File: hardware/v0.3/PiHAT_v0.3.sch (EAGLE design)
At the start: 37 parts, among them IC1 BMP280, J1 FTDI, J3 ISP, U1 ATMEGA328P, U2 TSL2561, U3 OPA344, U6 ADMP401, U7 SHT31/35, U8 CCS811, Y1 16MHZ

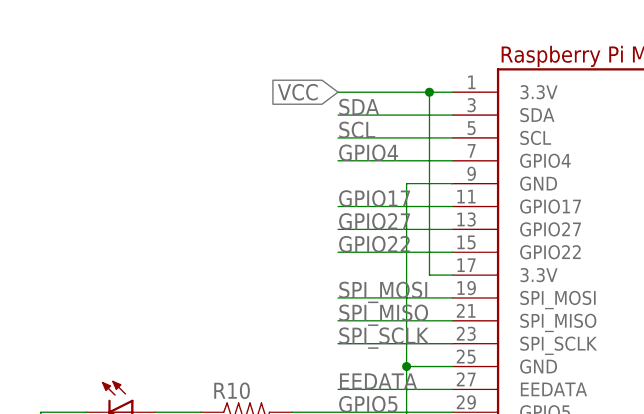
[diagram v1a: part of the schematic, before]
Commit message: Added jumpers on the I2C line
Jumpers between Pi's SDA and SCL lines and ATmega's SDA and SCL lines
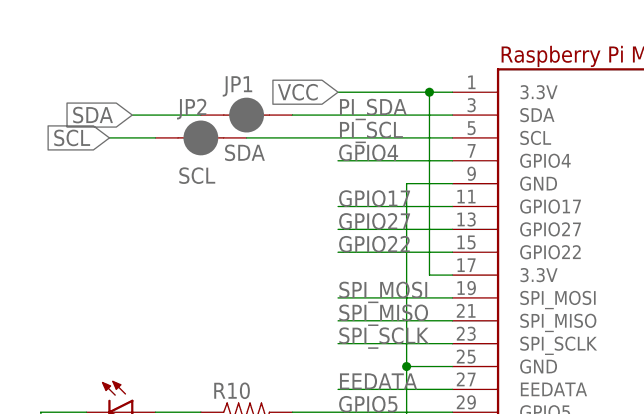
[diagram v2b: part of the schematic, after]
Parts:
- added JP1: SDA, SparkFun-Passives:JUMPER-PAD-2-NC_BY_PASTEFULL-BOX-SILK
- added JP2: SCL, SparkFun-Passives:JUMPER-PAD-2-NC_BY_PASTEFULL-BOX-SILK
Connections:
- new net PI_SCL: JP2.2, RPI1.SCL
- new net PI_SDA: JP1.2, RPI1.SDA
- net SCL: now also JP2.1; no longer RPI1.SCL
- net SDA: now also JP1.1; no longer RPI1.SDA
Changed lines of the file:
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@@
 <part name="C1" library="SparkFun-Passives" deviceset="CAP" device="0805" value="0.1uF"/>
 <part name="C6" library="SparkFun-Passives" deviceset="CAP" device="0805" value="0.1uF"/>
+<part name="JP1" library="SparkFun-Passives" deviceset="JUMPER-PAD-2-NC_BY_PASTE" device="FULL-BOX-SILK" value="SDA"/>
+<part name="JP2" library="SparkFun-Passives" deviceset="JUMPER-PAD-2-NC_BY_PASTE" device="FULL-BOX-SILK" value="SCL"/>
 </parts>
 <sheets>
@@
 <instance part="C1" gate="G$1" x="353.06" y="99.06"/>
 <instance part="C6" gate="G$1" x="289.56" y="104.14" rot="R180"/>
+<instance part="JP1" gate="G$1" x="182.88" y="121.92"/>
+<instance part="JP2" gate="G$1" x="177.8" y="119.38"/>
 </instances>
 <busses>
@@
 </segment>
 <segment>
-<pinref part="RPI1" gate="G$1" pin="SDA"/>
-<wire x1="205.74" y1="121.92" x2="193.04" y2="121.92" width="0.1524" layer="91"/>
-<label x="193.04" y="121.92" size="1.778" layer="95"/>
+<pinref part="JP1" gate="G$1" pin="1"/>
+<wire x1="177.8" y1="121.92" x2="170.18" y2="121.92" width="0.1524" layer="91"/>
+<label x="170.18" y="121.92" size="1.778" layer="95" rot="R180" xref="yes"/>
 </segment>
 </net>
@@
 </segment>
 <segment>
-<pinref part="RPI1" gate="G$1" pin="SCL"/>
-<wire x1="205.74" y1="119.38" x2="193.04" y2="119.38" width="0.1524" layer="91"/>
-<label x="193.04" y="119.38" size="1.778" layer="95"/>
+<pinref part="JP2" gate="G$1" pin="1"/>
+<wire x1="172.72" y1="119.38" x2="167.64" y2="119.38" width="0.1524" layer="91"/>
+<label x="167.64" y="119.38" size="1.778" layer="95" rot="R180" xref="yes"/>
 </segment>
 </net>
@@
 </segment>
 </net>
+<net name="PI_SDA" class="0">
+<segment>
+<pinref part="RPI1" gate="G$1" pin="SDA"/>
+<wire x1="205.74" y1="121.92" x2="187.96" y2="121.92" width="0.1524" layer="91"/>
+<label x="193.04" y="121.92" size="1.778" layer="95"/>
+<pinref part="JP1" gate="G$1" pin="2"/>
+</segment>
+</net>
+<net name="PI_SCL" class="0">
+<segment>
+<pinref part="RPI1" gate="G$1" pin="SCL"/>
+<wire x1="205.74" y1="119.38" x2="182.88" y2="119.38" width="0.1524" layer="91"/>
+<label x="193.04" y="119.38" size="1.778" layer="95"/>
+<pinref part="JP2" gate="G$1" pin="2"/>
+</segment>
+</net>

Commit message: BOM adjustments
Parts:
- removed C6: 0.1uF, SparkFun-Passives:CAP0805
- added C7: 0.1uF, SparkFun-Passives:CAP0805
- C11: DIGIKEY# (none) -> 311-1088-1-ND; MOUSER# (none) -> 603-CC603KRX7R7BB104; MPN (none) -> CC0603KRX7R7BB104
- C3: MOUSER# 603-RC0805FR-07100RL -> 603-CC603KRX7R7BB104
- renumbered C1 to C11
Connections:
- net GND: now also C7.2; no longer C6.1
- net VCC: now also C7.1; no longer C6.2
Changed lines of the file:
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@@
 <?xml version="1.0" encoding="utf-8"?>
 <!DOCTYPE eagle SYSTEM "eagle.dtd">
-<eagle version="7.7.0">
+<eagle version="7.6.0">
 <drawing>
 <settings>
@@
 <part name="C3" library="SparkFun-Passives" deviceset="CAP" device="0805" value="0.1uF">
 <attribute name="DIGIKEY#" value="311-1088-1-ND"/>
-<attribute name="MOUSER#" value="603-RC0805FR-07100RL"/>
+<attribute name="MOUSER#" value="603-CC603KRX7R7BB104"/>
 <attribute name="MPN" value="CC0603KRX7R7BB104"/>
 </part>
@@
 <part name="SUPPLY10" library="SparkFun-Aesthetics" deviceset="VCC" device=""/>
 <part name="SUPPLY13" library="SparkFun-Aesthetics" deviceset="VCC" device=""/>
-<part name="C1" library="SparkFun-Passives" deviceset="CAP" device="0805" value="0.1uF"/>
-<part name="C6" library="SparkFun-Passives" deviceset="CAP" device="0805" value="0.1uF"/>
 <part name="JP1" library="SparkFun-Passives" deviceset="JUMPER-PAD-2-NC_BY_PASTE" device="FULL-BOX-SILK" value="SDA"/>
 <part name="JP2" library="SparkFun-Passives" deviceset="JUMPER-PAD-2-NC_BY_PASTE" device="FULL-BOX-SILK" value="SCL"/>
+<part name="C7" library="SparkFun-Passives" deviceset="CAP" device="0805" value="0.1uF">
+<attribute name="DIGIKEY#" value="311-1088-1-ND"/>
+<attribute name="MOUSER#" value="603-CC603KRX7R7BB104"/>
+<attribute name="MPN" value="CC0603KRX7R7BB104"/>
+</part>
+<part name="C11" library="SparkFun-Passives" deviceset="CAP" device="0805" value="0.1uF">
+<attribute name="DIGIKEY#" value="311-1088-1-ND"/>
+<attribute name="MOUSER#" value="603-CC603KRX7R7BB104"/>
+<attribute name="MPN" value="CC0603KRX7R7BB104"/>
+</part>
 </parts>
 <sheets>
@@
 <instance part="SUPPLY10" gate="G$1" x="353.06" y="114.3"/>
 <instance part="SUPPLY13" gate="G$1" x="289.56" y="114.3"/>
-<instance part="C1" gate="G$1" x="353.06" y="99.06"/>
-<instance part="C6" gate="G$1" x="289.56" y="104.14" rot="R180"/>
 <instance part="JP1" gate="G$1" x="182.88" y="121.92"/>
 <instance part="JP2" gate="G$1" x="177.8" y="119.38"/>
+<instance part="C7" gate="G$1" x="289.56" y="101.6">
+<attribute name="DIGIKEY#" x="289.56" y="101.6" size="1.778" layer="96" display="off"/>
+<attribute name="MPN" x="289.56" y="101.6" size="1.778" layer="96" display="off"/>
+<attribute name="MOUSER#" x="289.56" y="101.6" size="1.778" layer="96" display="off"/>
+</instance>
+<instance part="C11" gate="G$1" x="353.06" y="99.06">
+<attribute name="DIGIKEY#" x="353.06" y="99.06" size="1.778" layer="96" display="off"/>
+<attribute name="MPN" x="353.06" y="99.06" size="1.778" layer="96" display="off"/>
+<attribute name="MOUSER#" x="353.06" y="99.06" size="1.778" layer="96" display="off"/>
+</instance>
 </instances>
 <busses>
@@
 <segment>
 <pinref part="IC1" gate="G$1" pin="GND"/>
-<pinref part="C6" gate="G$1" pin="1"/>
 <wire x1="297.18" y1="99.06" x2="289.56" y2="99.06" width="0.1524" layer="91"/>
 <wire x1="289.56" y1="99.06" x2="289.56" y2="91.44" width="0.1524" layer="91"/>
-<junction x="289.56" y="99.06"/>
 <wire x1="353.06" y1="91.44" x2="312.42" y2="91.44" width="0.1524" layer="91"/>
 <wire x1="312.42" y1="91.44" x2="289.56" y2="91.44" width="0.1524" layer="91"/>
@@
 <junction x="312.42" y="91.44"/>
 <label x="312.42" y="86.36" size="1.778" layer="95" rot="R270" xref="yes"/>
-<pinref part="C1" gate="G$1" pin="2"/>
 <wire x1="353.06" y1="91.44" x2="353.06" y2="96.52" width="0.1524" layer="91"/>
+<pinref part="C7" gate="G$1" pin="2"/>
+<junction x="289.56" y="99.06"/>
+<pinref part="C11" gate="G$1" pin="2"/>
 </segment>
 </net>
@@
 <wire x1="297.18" y1="109.22" x2="289.56" y2="109.22" width="0.1524" layer="91"/>
 <wire x1="289.56" y1="109.22" x2="289.56" y2="114.3" width="0.1524" layer="91"/>
-<pinref part="C6" gate="G$1" pin="2"/>
 <wire x1="289.56" y1="106.68" x2="289.56" y2="109.22" width="0.1524" layer="91"/>
 <junction x="289.56" y="109.22"/>
+<pinref part="C7" gate="G$1" pin="1"/>
 </segment>
 <segment>
@@
 <pinref part="SUPPLY10" gate="G$1" pin="VCC"/>
 <wire x1="353.06" y1="109.22" x2="353.06" y2="114.3" width="0.1524" layer="91"/>
-<pinref part="C1" gate="G$1" pin="1"/>
 <wire x1="353.06" y1="104.14" x2="353.06" y2="109.22" width="0.1524" layer="91"/>
 <junction x="353.06" y="109.22"/>
-</segment>
-</net>
+<pinref part="C11" gate="G$1" pin="1"/>
+</segment>
+</net>

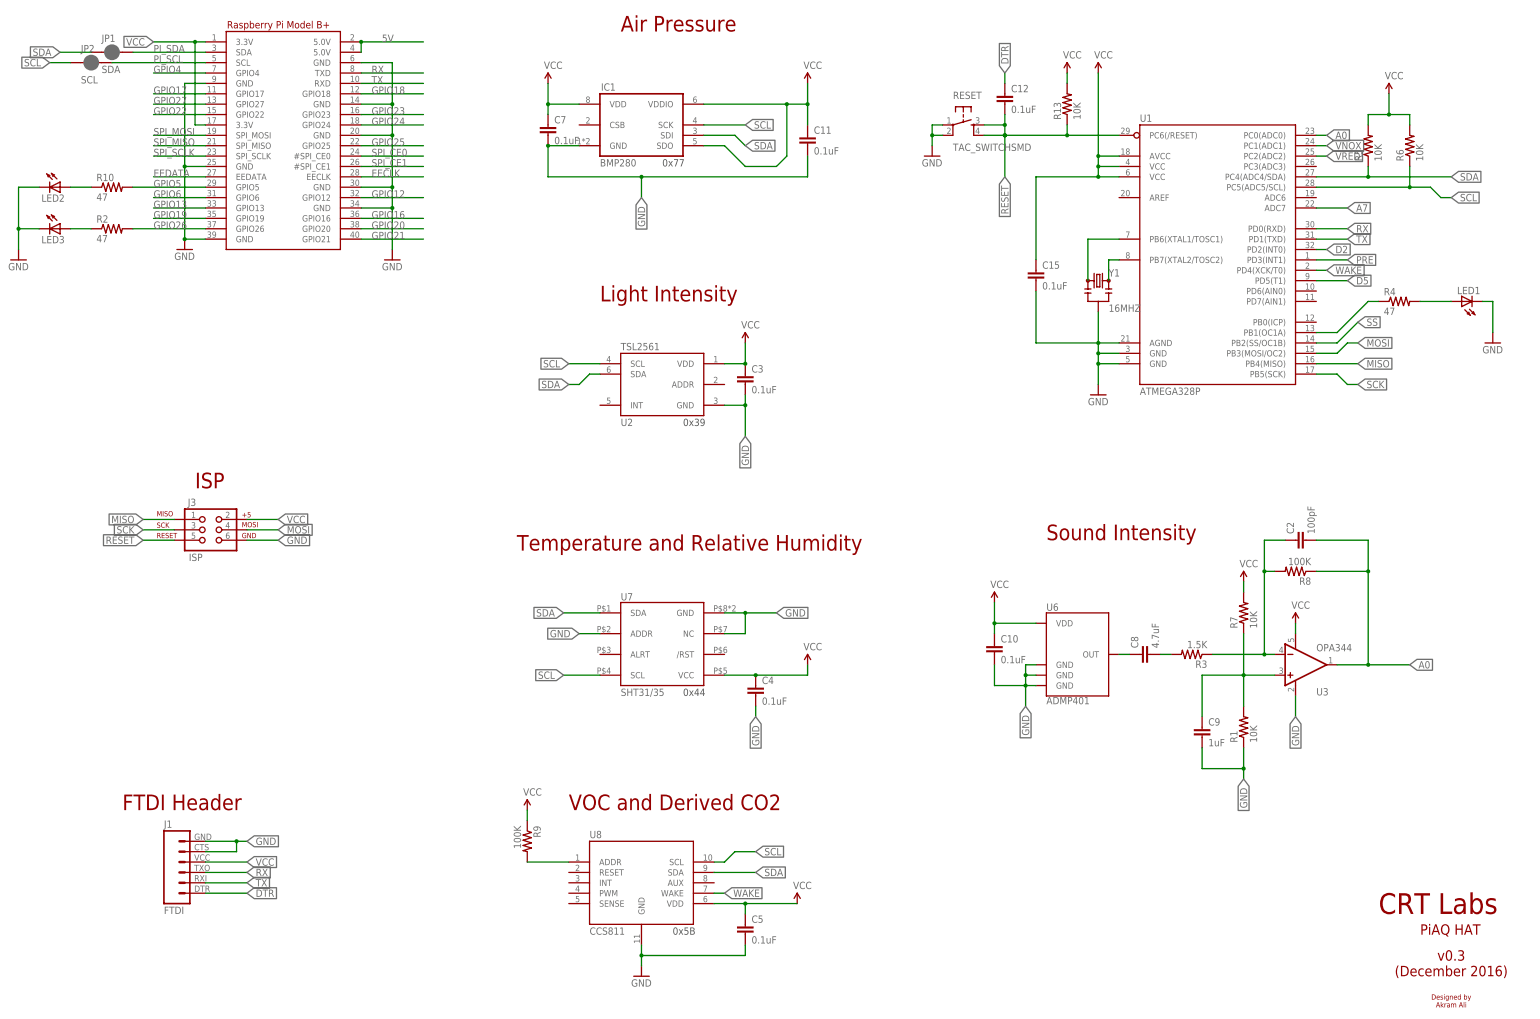
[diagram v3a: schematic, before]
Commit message: Updated all attributes for BOM
Fixed digikey and mouser numbers
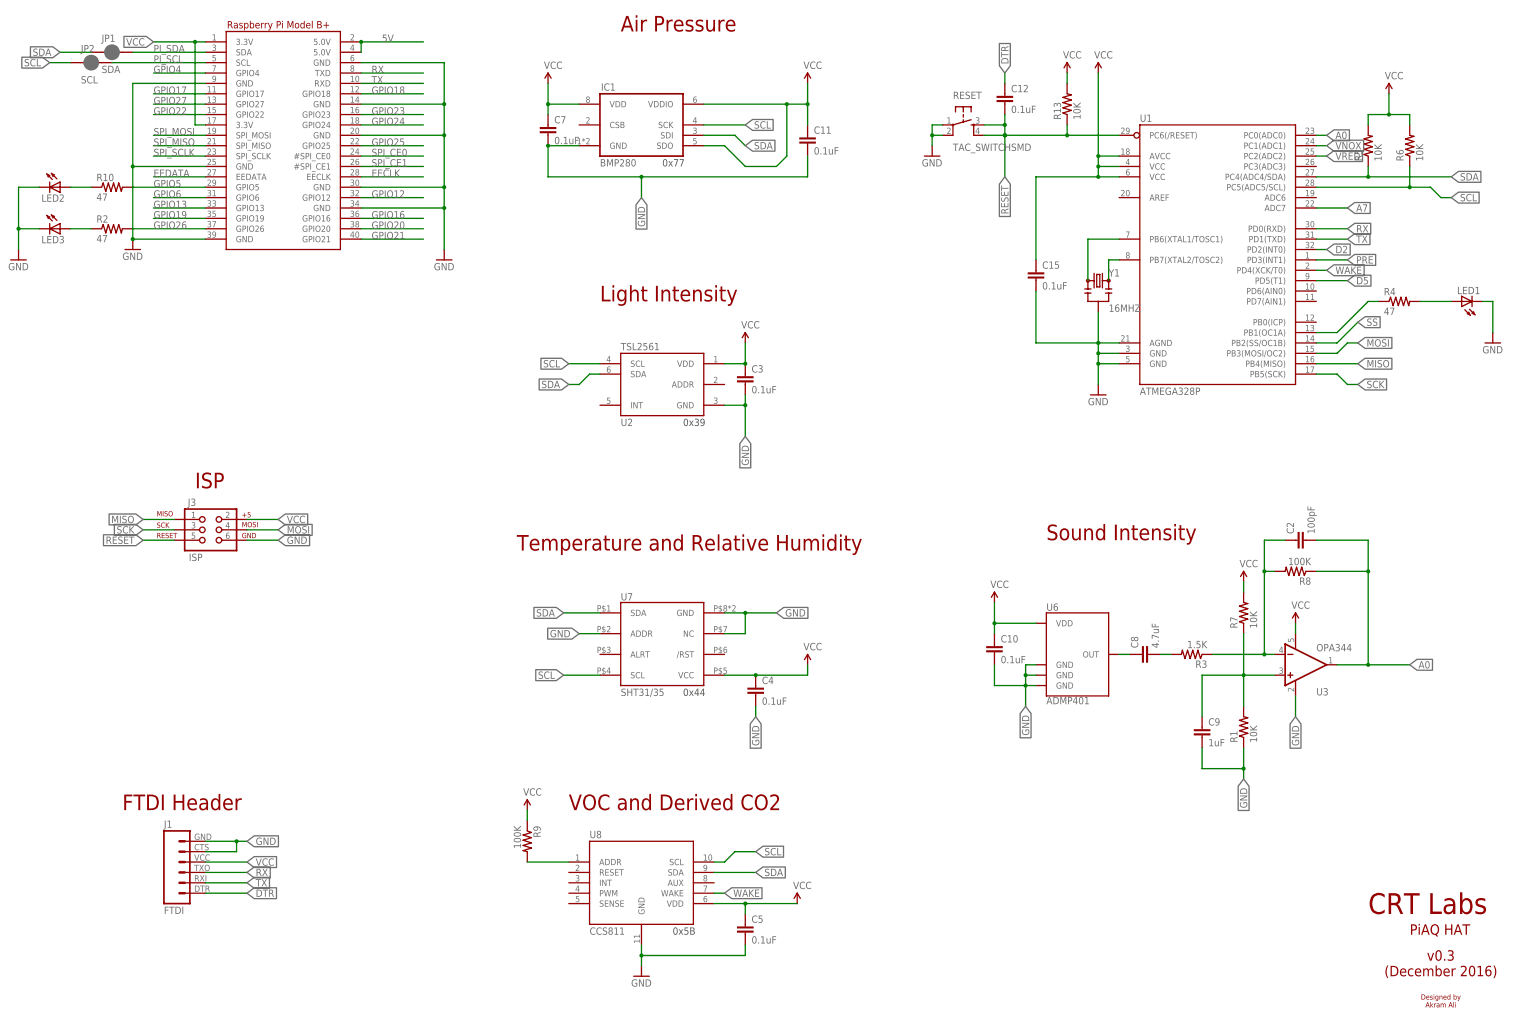
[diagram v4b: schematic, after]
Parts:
- IC1: DIGIKEY# (none) -> 828-1064-1-ND; MANF (none) -> BMP280; MOUSER# (none) -> 262-BMP280
- J1: DIGIKEY# 768-1129-1-ND -> (none); MOUSER# 895-FT231XS-R -> (none); MPN FT231XS-R -> (none); NO_BOM (none) -> TRUE
- R8, R9: DIGIKEY# 541-82.0CCT-ND -> 311-100KCRCT-ND
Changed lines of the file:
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@@
 </part>
 <part name="R8" library="SparkFun-Passives" deviceset="RESISTOR" device="0805-RES" value="100K">
-<attribute name="DIGIKEY#" value="541-82.0CCT-ND"/>
+<attribute name="DIGIKEY#" value="311-100KCRCT-ND"/>
 <attribute name="MOUSER#" value="603-RC0805FR-07100KL"/>
 <attribute name="MPN" value="RC0805FR-07100KL"/>
@@
 <part name="SUPPLY8" library="SparkFun-Aesthetics" deviceset="VCC" device=""/>
 <part name="R9" library="SparkFun-Passives" deviceset="RESISTOR" device="0805-RES" value="100K">
-<attribute name="DIGIKEY#" value="541-82.0CCT-ND"/>
+<attribute name="DIGIKEY#" value="311-100KCRCT-ND"/>
 <attribute name="MOUSER#" value="603-RC0805FR-07100KL"/>
 <attribute name="MPN" value="RC0805FR-07100KL"/>
@@
 </part>
 <part name="J1" library="SparkFun-Connectors" deviceset="FTDI_BASIC" device="PTH" value="FTDI">
-<attribute name="DIGIKEY#" value="768-1129-1-ND"/>
-<attribute name="MOUSER#" value="895-FT231XS-R"/>
-<attribute name="MPN" value="FT231XS-R"/>
+<attribute name="NO_BOM" value="TRUE"/>
 </part>
 <part name="J3" library="SparkFun-Connectors" deviceset="AVR_SPI_PRG_6" device="PTH" value="ISP">
 <attribute name="NO_BOM" value="TRUE"/>
 </part>
-<part name="IC1" library="bosch-bmp280" deviceset="BMP280" device=""/>
+<part name="IC1" library="bosch-bmp280" deviceset="BMP280" device="">
+<attribute name="DIGIKEY#" value="828-1064-1-ND"/>
+<attribute name="MANF" value="BMP280"/>
+<attribute name="MOUSER#" value="262-BMP280"/>
+</part>
 <part name="SUPPLY10" library="SparkFun-Aesthetics" deviceset="VCC" device=""/>
 <part name="SUPPLY13" library="SparkFun-Aesthetics" deviceset="VCC" device=""/>
@@
 <text x="281.94" y="0" size="3.81" layer="94">Temperature and Relative Humidity</text>
 <text x="203.2" y="15.24" size="3.81" layer="94">ISP</text>
-<text x="492.76" y="-88.9" size="5.08" layer="94" font="vector" ratio="20">CRT Labs</text>
-<text x="502.92" y="-93.98" size="2.54" layer="94" font="vector" ratio="10">PiAQ HAT</text>
-<text x="510.54" y="-104.14" size="2.54" layer="94" font="vector" ratio="10" align="bottom-center">v0.3
+<text x="490.22" y="-88.9" size="5.08" layer="94" font="vector" ratio="20">CRT Labs</text>
+<text x="500.38" y="-93.98" size="2.54" layer="94" font="vector" ratio="10">PiAQ HAT</text>
+<text x="508" y="-104.14" size="2.54" layer="94" font="vector" ratio="10" align="bottom-center">v0.3
 (December 2016)</text>
-<text x="510.54" y="-111.76" size="1.27" layer="94" font="vector" ratio="10" align="bottom-center">Designed by
+<text x="508" y="-111.76" size="1.27" layer="94" font="vector" ratio="10" align="bottom-center">Designed by
 Akram Ali</text>
 <text x="322.58" y="30.48" size="1.778" layer="97">0x39</text>
@@
 <attribute name="NO_BOM" x="223.52" y="104.14" size="1.778" layer="96" display="off"/>
 </instance>
-<instance part="GND1" gate="1" x="200.66" y="73.66"/>
-<instance part="GND2" gate="1" x="251.46" y="71.12"/>
+<instance part="GND1" gate="1" x="187.96" y="73.66"/>
+<instance part="GND2" gate="1" x="264.16" y="71.12"/>
 <instance part="U1" gate="U$1" x="454.66" y="71.12">
 <attribute name="MPN" x="454.66" y="71.12" size="1.778" layer="96" rot="R270" display="off"/>
@@
 </instance>
 <instance part="J1" gate="G$1" x="200.66" y="-78.74">
-<attribute name="MPN" x="200.66" y="-78.74" size="1.778" layer="96" display="off"/>
-<attribute name="DIGIKEY#" x="200.66" y="-78.74" size="1.778" layer="96" display="off"/>
-<attribute name="MOUSER#" x="200.66" y="-78.74" size="1.778" layer="96" display="off"/>
+<attribute name="NO_BOM" x="200.66" y="-78.74" size="1.778" layer="96" display="off"/>
 </instance>
 <instance part="J3" gate="G$1" x="205.74" y="5.08">
 <attribute name="NO_BOM" x="205.74" y="5.08" size="1.778" layer="96" display="off"/>
 </instance>
-<instance part="IC1" gate="G$1" x="312.42" y="104.14"/>
+<instance part="IC1" gate="G$1" x="312.42" y="104.14">
+<attribute name="DIGIKEY#" x="312.42" y="104.14" size="1.778" layer="96" display="off"/>
+<attribute name="MANF" x="312.42" y="104.14" size="1.778" layer="96" display="off"/>
+<attribute name="MOUSER#" x="312.42" y="104.14" size="1.778" layer="96" display="off"/>
+</instance>
 <instance part="SUPPLY10" gate="G$1" x="353.06" y="114.3"/>
 <instance part="SUPPLY13" gate="G$1" x="289.56" y="114.3"/>
@@
 <pinref part="RPI1" gate="G$1" pin="GND@3"/>
 <pinref part="GND1" gate="1" pin="GND"/>
-<wire x1="200.66" y1="93.98" x2="205.74" y2="93.98" width="0.1524" layer="91"/>
-<wire x1="205.74" y1="76.2" x2="200.66" y2="76.2" width="0.1524" layer="91"/>
-<wire x1="200.66" y1="93.98" x2="200.66" y2="76.2" width="0.1524" layer="91"/>
-<junction x="200.66" y="76.2"/>
+<wire x1="187.96" y1="93.98" x2="205.74" y2="93.98" width="0.1524" layer="91"/>
+<wire x1="205.74" y1="76.2" x2="187.96" y2="76.2" width="0.1524" layer="91"/>
+<wire x1="187.96" y1="93.98" x2="187.96" y2="76.2" width="0.1524" layer="91"/>
+<junction x="187.96" y="76.2"/>
 <pinref part="RPI1" gate="G$1" pin="GND@4"/>
-<wire x1="200.66" y1="114.3" x2="205.74" y2="114.3" width="0.1524" layer="91"/>
-<wire x1="200.66" y1="93.98" x2="200.66" y2="114.3" width="0.1524" layer="91"/>
-<junction x="200.66" y="93.98"/>
+<wire x1="187.96" y1="114.3" x2="205.74" y2="114.3" width="0.1524" layer="91"/>
+<wire x1="187.96" y1="93.98" x2="187.96" y2="114.3" width="0.1524" layer="91"/>
+<junction x="187.96" y="93.98"/>
 <pinref part="RPI1" gate="G$1" pin="GND@5"/>
 </segment>
@@
 <pinref part="RPI1" gate="G$1" pin="GND"/>
 <pinref part="GND2" gate="1" pin="GND"/>
-<wire x1="243.84" y1="119.38" x2="251.46" y2="119.38" width="0.1524" layer="91"/>
-<wire x1="251.46" y1="119.38" x2="251.46" y2="109.22" width="0.1524" layer="91"/>
+<wire x1="243.84" y1="119.38" x2="264.16" y2="119.38" width="0.1524" layer="91"/>
+<wire x1="264.16" y1="119.38" x2="264.16" y2="109.22" width="0.1524" layer="91"/>
 <pinref part="RPI1" gate="G$1" pin="GND@7"/>
-<wire x1="251.46" y1="109.22" x2="251.46" y2="101.6" width="0.1524" layer="91"/>
-<wire x1="251.46" y1="101.6" x2="251.46" y2="88.9" width="0.1524" layer="91"/>
-<wire x1="251.46" y1="88.9" x2="251.46" y2="83.82" width="0.1524" layer="91"/>
-<wire x1="251.46" y1="83.82" x2="251.46" y2="73.66" width="0.1524" layer="91"/>
-<wire x1="243.84" y1="83.82" x2="251.46" y2="83.82" width="0.1524" layer="91"/>
-<junction x="251.46" y="83.82"/>
+<wire x1="264.16" y1="109.22" x2="264.16" y2="101.6" width="0.1524" layer="91"/>
+<wire x1="264.16" y1="101.6" x2="264.16" y2="88.9" width="0.1524" layer="91"/>
+<wire x1="264.16" y1="88.9" x2="264.16" y2="83.82" width="0.1524" layer="91"/>
+<wire x1="264.16" y1="83.82" x2="264.16" y2="73.66" width="0.1524" layer="91"/>
+<wire x1="243.84" y1="83.82" x2="264.16" y2="83.82" width="0.1524" layer="91"/>
+<junction x="264.16" y="83.82"/>
 <pinref part="RPI1" gate="G$1" pin="GND@6"/>
-<wire x1="243.84" y1="88.9" x2="251.46" y2="88.9" width="0.1524" layer="91"/>
-<junction x="251.46" y="88.9"/>
+<wire x1="243.84" y1="88.9" x2="264.16" y2="88.9" width="0.1524" layer="91"/>
+<junction x="264.16" y="88.9"/>
 <pinref part="RPI1" gate="G$1" pin="GND@2"/>
-<wire x1="243.84" y1="101.6" x2="251.46" y2="101.6" width="0.1524" layer="91"/>
-<junction x="251.46" y="101.6"/>
+<wire x1="243.84" y1="101.6" x2="264.16" y2="101.6" width="0.1524" layer="91"/>
+<junction x="264.16" y="101.6"/>
 <pinref part="RPI1" gate="G$1" pin="GND@1"/>
-<wire x1="243.84" y1="109.22" x2="251.46" y2="109.22" width="0.1524" layer="91"/>
-<junction x="251.46" y="109.22"/>
-</segment>
-<segment>
+<wire x1="243.84" y1="109.22" x2="264.16" y2="109.22" width="0.1524" layer="91"/>
+<junction x="264.16" y="109.22"/>
+</segment>
+<segment>
